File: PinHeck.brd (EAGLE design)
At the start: 359.2 x 152.3 mm, 337 parts, among them IC1 FT232RL-REEL, IC2 PIC32MX795F512L-80I/PT, IC3 CD74HCT244E, IC4 CD74HCT244E, IC5 ULN2803A, J1 500075-1517, J11 No Load, J2 500075-1517, J3 N/A, J6 161-3507-E, P1 TC33X-2-103E, SW1 101-0134-EV, SW2 101-0134-EV, U1 P8X32A-Q44, U10 74HCT2G04GV,125, U11 74HC165D,652, U12 74HC165D,652, U14 MC74HC08ADG, U15 MC74HC08ADG, U16 MC74HC08ADG, U17 MC74HC08ADG, U18 MC74HC08ADG, U19 MC74HC08ADG, U2 FT230XS-R, U20 TIP107, U21 TIP107, U22 TIP107, U23 TIP107, U24 TIP107, U25 TIP107, U26 TIP107, U27 TIP107, U28 TIP102, U29 TIP102, U3 74HC595D-Q100, U30 TIP102, U31 TIP102, U32 TIP102, U33 TIP102, U34 TIP102, U35 TIP102, U36 WS2801, U37 TIP102, U38 WS2801, U39 LM2937IMP-3.3/NOPB, U4 24LC1025-I/P, U40 TIP102, U41 TIP102, U42 TIP102, U43 TIP102, U44 TIP102, U45 TIP102, U46 TIP102, U47 TIP102, U48 TIP102, U49 TIP102, U5 74HC595D-Q100, U50 TIP102, U51 TIP102, U52 CD74HC123M96, U6 TIP102, U7 TIP102, U8 TIP102, U9 TIP102, X1 FQ7050B-8.000, X2 ECS-65-20-4X

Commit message: Updated Bill of Materials.
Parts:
- BOARD_POWER, SOL_PWR: value 26-62-4040 -> 26-60-4040
- C10: device PP_Passives:0805 -> PP_Passives:1206
- moved C10 0.80 mm to (95.8, 105.9)
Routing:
- net GND: track 54.5 -> 52.0 mm
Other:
- outline, holes or cut-outs redrawn
- board text added: "REV: 5"
- board text removed: "REV: 6"
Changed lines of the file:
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@@
 <?xml version="1.0" encoding="utf-8"?>
 <!DOCTYPE eagle SYSTEM "eagle.dtd">
-<eagle version="6.3">
+<eagle version="6.5.0">
 <drawing>
 <settings>
@@
 <wire x1="339.09" y1="174.371" x2="339.09" y2="22.098" width="0.4064" layer="20"/>
 <wire x1="339.09" y1="22.098" x2="-20.066" y2="22.098" width="0.4064" layer="20"/>
-<wire x1="-20.066" y1="22.098" x2="-20.066" y2="174.117" width="0.4064" layer="20"/>
-<wire x1="-20.066" y1="174.117" x2="-20.066" y2="174.371" width="0.4064" layer="20"/>
+<wire x1="-20.066" y1="22.098" x2="-20.066" y2="174.371" width="0.4064" layer="20"/>
 <text x="50.292" y="166.624" size="1.4224" layer="21" font="vector">PIC USB</text>
 <text x="80.518" y="158.242" size="1.016" layer="21" font="vector" rot="R90">AC_46</text>
@@
 <text x="316.992" y="110.998" size="0.8128" layer="21" font="vector">GND</text>
 <text x="235.204" y="108.712" size="1.016" layer="21">PinHeck Pinball System</text>
-<text x="235.204" y="107.188" size="1.016" layer="21">REV: 6</text>
+<text x="235.204" y="107.188" size="1.016" layer="21">REV: 5</text>
 <text x="235.204" y="102.362" size="1.016" layer="21">Designers:</text>
 <text x="235.204" y="105.664" size="1.016" layer="21">www.benheck.com</text>
@@
 <element name="C9" library="PP_Passives" package="0805" value=".1uF" x="104.648" y="133.096" rot="R180"/>
 <element name="C11" library="PP_Passives" package="0805" value=".1uF" x="86.614" y="133.858" rot="R180"/>
-<element name="C10" library="PP_Passives" package="0805" value="10uF" x="96.012" y="106.68" smashed="yes" rot="R270">
-<attribute name="NAME" x="95.123" y="104.2035" size="0.8128" layer="25" font="vector"/>
+<element name="C10" library="PP_Passives" package="1206" value="10uF" x="95.758" y="105.918" smashed="yes" rot="R270">
+<attribute name="NAME" x="93.345" y="108.5215" size="0.8128" layer="25" font="vector"/>
 </element>
 <element name="R12" library="PP_Passives" package="0805" value="50" x="125.222" y="115.57"/>
@@
 <element name="F2" library="PP_Passives" package="4245K" value="4245K" x="257.048" y="66.294" rot="R270"/>
 <element name="F3" library="PP_Passives" package="4245K" value="4245K" x="269.24" y="66.294" rot="R270"/>
-<element name="SOL_PWR" library="PP_Connectors" package="MOLEX_KK_4" value="26-62-4040" x="257.556" y="28.702" smashed="yes">
+<element name="SOL_PWR" library="PP_Connectors" package="MOLEX_KK_4" value="26-60-4040" x="257.556" y="28.702" smashed="yes">
 <attribute name="NAME" x="252.857" y="35.941" size="1.4224" layer="25" font="vector"/>
 </element>
@@
 <element name="C46" library="PP_Passives" package="0805" value=".1uF" x="227.33" y="133.858" rot="R270"/>
 <element name="C47" library="PP_Passives" package="0805" value=".1uF" x="193.04" y="133.858" rot="R270"/>
-<element name="BOARD_POWER" library="PP_Connectors" package="MOLEX_KK_4" value="26-62-4040" x="18.288" y="167.894" smashed="yes">
+<element name="BOARD_POWER" library="PP_Connectors" package="MOLEX_KK_4" value="26-60-4040" x="18.288" y="167.894" smashed="yes">
 <attribute name="NAME" x="10.033" y="160.909" size="1.4224" layer="25" font="vector"/>
 </element>
@@
 <wire x1="98.844" y1="127.35" x2="98.844" y2="132.372" width="0.1778" layer="1"/>
 <wire x1="98.844" y1="132.372" x2="99.314" y2="132.842" width="0.1778" layer="1"/>
-<wire x1="99.314" y1="132.842" x2="100.584" y2="132.842" width="0.1778" layer="1"/>
-<wire x1="100.584" y1="132.842" x2="101.092" y2="132.842" width="0.1778" layer="1"/>
-<wire x1="101.23" y1="133.488" x2="101.23" y2="133.858" width="0.1778" layer="1"/>
 <wire x1="103.748" y1="133.096" x2="103.494" y2="132.842" width="0.1778" layer="1"/>
-<wire x1="103.494" y1="132.842" x2="101.092" y2="132.842" width="0.1778" layer="1"/>
-<wire x1="101.23" y1="133.488" x2="101.23" y2="132.842" width="0.1778" layer="1"/>
-<wire x1="101.23" y1="132.842" x2="100.584" y2="132.842" width="0.1778" layer="1"/>
+<wire x1="103.494" y1="132.842" x2="99.314" y2="132.842" width="0.1778" layer="1"/>
+<wire x1="101.23" y1="133.858" x2="101.23" y2="132.842" width="0.1778" layer="1"/>
+<wire x1="101.23" y1="132.842" x2="101.092" y2="132.842" width="0.1778" layer="1"/>
 <wire x1="100.844" y1="127.35" x2="100.838" y2="127.344" width="0.1778" layer="1"/>
-<wire x1="100.838" y1="127.344" x2="100.838" y2="125.73" width="0.1778" layer="1"/>
-<wire x1="100.838" y1="125.73" x2="100.838" y2="129.286" width="0.1778" layer="1"/>
+<wire x1="100.838" y1="127.344" x2="100.838" y2="129.286" width="0.1778" layer="1"/>
 <wire x1="100.838" y1="129.286" x2="101.6" y2="130.048" width="0.1778" layer="1"/>
 <via x="102.616" y="133.35" extent="1-16" drill="0.5" diameter="0.8048"/>
 <via x="107.188" y="133.35" extent="1-16" drill="0.5" diameter="0.8048"/>
 <wire x1="104.744" y1="121.45" x2="103.67" y2="121.45" width="0.1778" layer="1"/>
-<wire x1="103.67" y1="121.45" x2="103.378" y2="121.158" width="0.1778" layer="1"/>
-<wire x1="100.838" y1="125.73" x2="100.838" y2="121.412" width="0.1778" layer="1"/>
+<wire x1="100.838" y1="127.344" x2="100.838" y2="121.412" width="0.1778" layer="1"/>
 <wire x1="100.838" y1="121.412" x2="101.6" y2="120.65" width="0.1778" layer="1"/>
 <wire x1="101.6" y1="120.65" x2="102.87" y2="120.65" width="0.1778" layer="1"/>
-<wire x1="102.87" y1="120.65" x2="103.378" y2="121.158" width="0.1778" layer="1"/>
+<wire x1="102.87" y1="120.65" x2="103.67" y2="121.45" width="0.1778" layer="1"/>
 <via x="122.428" y="125.73" extent="1-16" drill="0.5" diameter="0.8048"/>
 <via x="122.682" y="119.888" extent="1-16" drill="0.5" diameter="0.8048"/>
@@
 <contactref element="C50" pad="NEG"/>
 <via x="127" y="120.65" extent="1-16" drill="0.5" diameter="0.8048"/>
-<via x="94.742" y="105.664" extent="1-16" drill="0.5" diameter="0.8048"/>
-<via x="94.742" y="106.934" extent="1-16" drill="0.5" diameter="0.8048"/>
-<via x="94.742" y="108.204" extent="1-16" drill="0.5" diameter="0.8048"/>
+<via x="93.726" y="105.664" extent="1-16" drill="0.5" diameter="0.8048"/>
+<via x="93.726" y="104.14" extent="1-16" drill="0.5" diameter="0.8048"/>
+<via x="93.726" y="107.442" extent="1-16" drill="0.5" diameter="0.8048"/>
 <via x="104.14" y="105.41" extent="1-16" drill="0.5" diameter="0.8048"/>
 <via x="89.662" y="114.808" extent="1-16" drill="0.5" diameter="0.8048"/>
@@
 <via x="109.347" y="124.9045" extent="1-16" drill="0.5" diameter="0.8048"/>
 <via x="111.379" y="124.9045" extent="1-16" drill="0.5" diameter="0.8048"/>
-<wire x1="111.39" y1="121.45" x2="110.998" y2="121.45" width="0.1778" layer="1"/>
 <via x="112.395" y="121.8565" extent="1-16" drill="0.5" diameter="0.8048"/>
-<wire x1="110.998" y1="121.45" x2="104.744" y2="121.45" width="0.1778" layer="1"/>
+<wire x1="111.39" y1="121.45" x2="104.744" y2="121.45" width="0.1778" layer="1"/>
 <wire x1="111.39" y1="121.45" x2="112.268" y2="121.45" width="0.1778" layer="1"/>
 <wire x1="112.268" y1="121.45" x2="112.268" y2="121.92" width="0.1778" layer="1"/>
 <wire x1="111.39" y1="122.428" x2="111.39" y2="121.45" width="0.1778" layer="1"/>
-<wire x1="111.39" y1="121.45" x2="110.998" y2="121.45" width="0.1778" layer="1"/>
 <via x="104.902" y="113.792" extent="1-16" drill="0.5" diameter="0.8048"/>
 <via x="93.218" y="115.824" extent="1-16" drill="0.5" diameter="0.8048"/>
@@
 <contactref element="IC2" pad="85"/>
 <contactref element="C10" pad="1"/>
-<wire x1="96.012" y1="107.58" x2="96.012" y2="107.9801" width="0.2032" layer="1"/>
+<wire x1="95.758" y1="107.318" x2="96.012" y2="107.9801" width="0.2032" layer="1"/>
 <wire x1="96.844" y1="113.95" x2="96.844" y2="108.8121" width="0.2032" layer="1"/>
 <wire x1="96.844" y1="108.8121" x2="96.012" y2="107.9801" width="0.2032" layer="1"/>
@@
 <contactref element="R51" pad="2"/>
 <contactref element="IC2" pad="74"/>
-<wire x1="152.7835" y1="78.867" x2="153.0477" y2="78.867" width="0.254" layer="1"/>
 <wire x1="153.0477" y1="78.867" x2="153.924" y2="79.7433" width="0.254" layer="1"/>
 <wire x1="153.924" y1="79.7433" x2="153.924" y2="83.174" width="0.254" layer="1"/>
-<wire x1="151.504" y1="78.867" x2="152.7835" y2="78.867" width="0.254" layer="1"/>
-<wire x1="153.5843" y1="83.8535" x2="153.924" y2="83.5138" width="0.254" layer="1"/>
+<wire x1="151.504" y1="78.867" x2="153.0477" y2="78.867" width="0.254" layer="1"/>
 <wire x1="153.924" y1="83.5138" x2="153.924" y2="83.174" width="0.254" layer="1"/>
-<via x="89.408" y="104.648" extent="1-16" drill="0.5" diameter="0.8048"/>
+<via x="91.694" y="102.362" extent="1-16" drill="0.5" diameter="0.8048"/>
 <via x="87.884" y="114.3" extent="1-16" drill="0.5" diameter="0.8048"/>
-<wire x1="89.408" y1="104.648" x2="106.934" y2="104.648" width="0.254" layer="1"/>
-<wire x1="106.934" y1="104.648" x2="120.396" y2="91.186" width="0.254" layer="1"/>
+<wire x1="91.694" y1="102.362" x2="109.22" y2="102.362" width="0.254" layer="1"/>
+<wire x1="109.22" y1="102.362" x2="120.396" y2="91.186" width="0.254" layer="1"/>
 <wire x1="120.396" y1="91.186" x2="152.294790625" y2="91.186" width="0.254" layer="1"/>
 <wire x1="152.294790625" y1="91.186" x2="152.654" y2="90.826790625" width="0.254" layer="1"/>
 <wire x1="152.654" y1="90.826790625" x2="152.654" y2="84.7838" width="0.254" layer="1"/>
-<wire x1="152.654" y1="84.7838" x2="153.5843" y2="83.8535" width="0.254" layer="1"/>
+<wire x1="152.654" y1="84.7838" x2="153.924" y2="83.5138" width="0.254" layer="1"/>
 <wire x1="87.884" y1="114.3" x2="87.884" y2="106.172" width="0.254" layer="16"/>
-<wire x1="87.884" y1="106.172" x2="89.408" y2="104.648" width="0.254" layer="16"/>
+<wire x1="87.884" y1="106.172" x2="91.694" y2="102.362" width="0.254" layer="16"/>
 <wire x1="91.344" y1="116.25" x2="89.834" y2="116.25" width="0.1778" layer="1"/>
 <wire x1="89.834" y1="116.25" x2="87.884" y2="114.3" width="0.1778" layer="1"/>

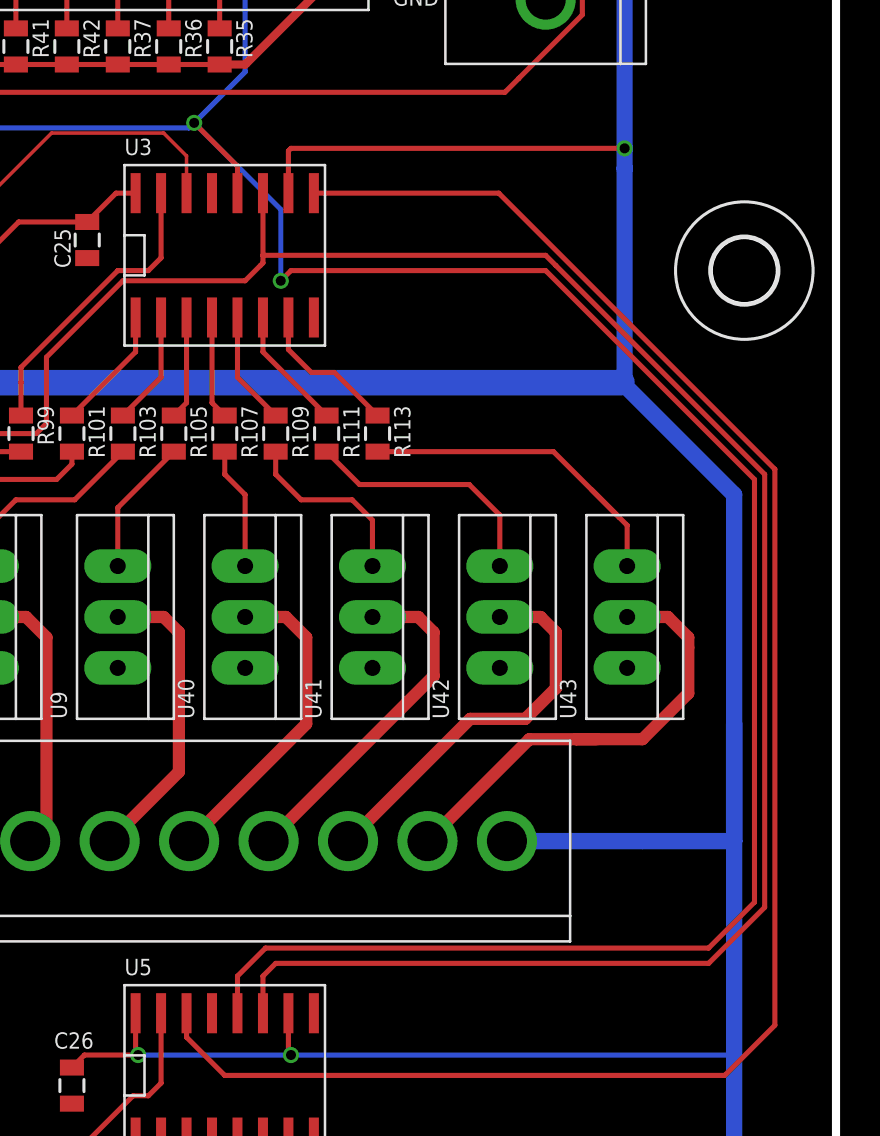
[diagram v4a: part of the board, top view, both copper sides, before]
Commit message: Swapped LAT and CLK on 595. FIXED.
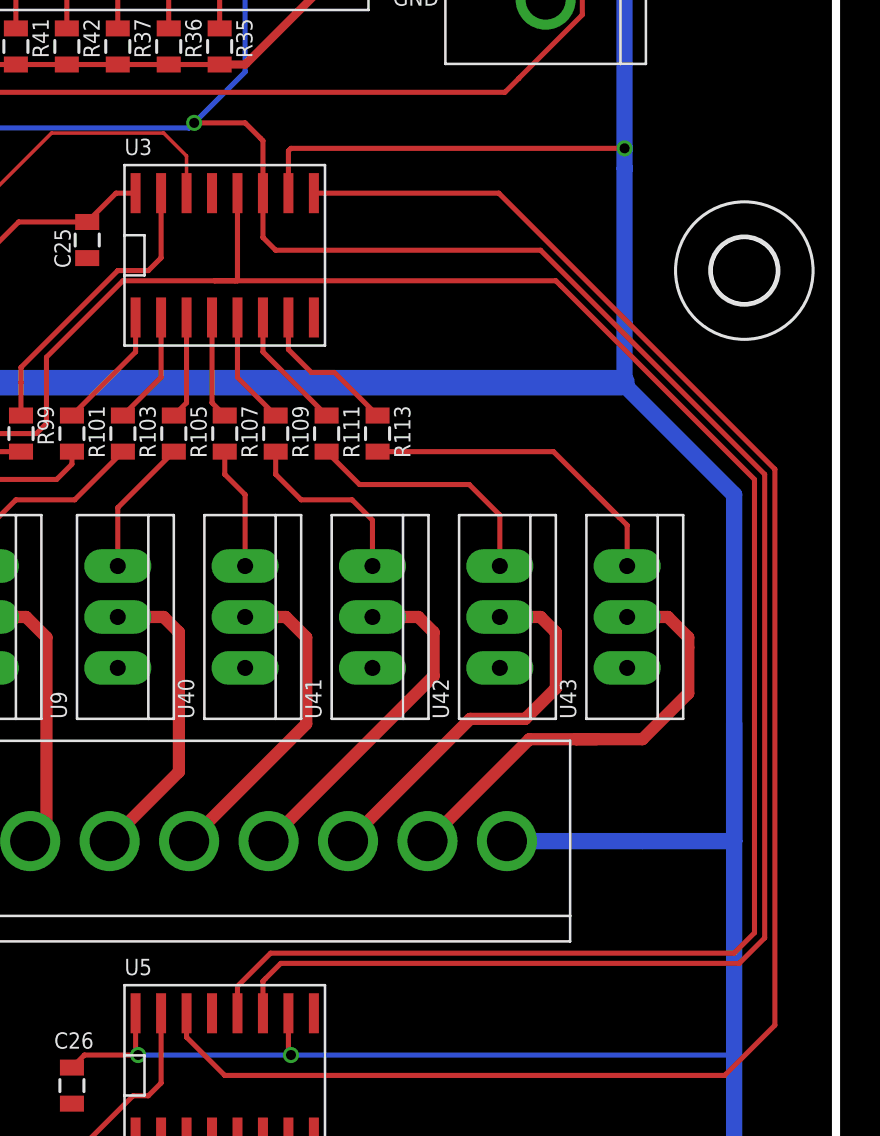
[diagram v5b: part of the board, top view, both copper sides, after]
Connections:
- net !DATA_LAT: now also U3.12, U5.12; no longer U3.11, U5.11
- net DATA_CLK: now also U3.11, U5.11; no longer U3.12, U5.12
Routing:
- net DATA_CLK: track 365.2 -> 361.9 mm, vias 4 -> 3
- net !DATA_LAT: track 115.6 -> 117.4 mm
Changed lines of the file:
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@@
 </signal>
 <signal name="DATA_CLK">
-<contactref element="U3" pad="12"/>
-<contactref element="U5" pad="12"/>
 <contactref element="U11" pad="2"/>
 <contactref element="U12" pad="2"/>
@@
 <wire x1="307.288" y1="129.413" x2="308.991" y2="129.413" width="0.254" layer="1"/>
 <wire x1="308.991" y1="129.413" x2="309.118" y2="129.286" width="0.254" layer="1" curve="-90"/>
-<wire x1="307.086" y1="105.156" x2="309.245" y2="102.997" width="0.254" layer="1"/>
-<wire x1="309.245" y1="102.997" x2="309.245" y2="101.652" width="0.254" layer="1"/>
 <wire x1="309.626" y1="115.062" x2="309.626" y2="110.744" width="0.254" layer="16"/>
 <wire x1="309.626" y1="110.744" x2="309.626" y2="107.696" width="0.254" layer="16"/>
 <wire x1="309.626" y1="107.696" x2="307.086" y2="105.156" width="0.254" layer="16"/>
 <via x="307.086" y="105.156" extent="1-16" drill="0.5"/>
-<wire x1="309.245" y1="60.758" x2="309.245" y2="62.611" width="0.254" layer="1"/>
-<wire x1="309.245" y1="62.611" x2="310.642" y2="64.008" width="0.254" layer="1"/>
-<wire x1="310.642" y1="64.008" x2="332.74" y2="64.008" width="0.254" layer="1"/>
-<wire x1="332.74" y1="64.008" x2="335.026" y2="66.294" width="0.254" layer="1"/>
-<wire x1="335.026" y1="66.294" x2="335.026" y2="87.376" width="0.254" layer="1"/>
-<wire x1="335.026" y1="87.376" x2="324.612" y2="97.79" width="0.254" layer="1"/>
-<wire x1="324.612" y1="97.79" x2="311.912" y2="97.79" width="0.254" layer="1"/>
-<wire x1="311.912" y1="97.79" x2="311.404" y2="97.282" width="0.254" layer="1"/>
-<via x="311.404" y="97.282" extent="1-16" drill="0.5"/>
-<wire x1="311.404" y1="97.282" x2="311.404" y2="100.838" width="0.254" layer="16"/>
-<wire x1="311.404" y1="100.838" x2="307.086" y2="105.156" width="0.254" layer="16"/>
 <wire x1="283.21" y1="104.902" x2="290.83" y2="104.902" width="0.254" layer="16"/>
 <wire x1="290.83" y1="104.902" x2="306.832" y2="104.902" width="0.254" layer="16"/>
 <wire x1="306.832" y1="104.902" x2="307.086" y2="105.156" width="0.254" layer="16"/>
+<contactref element="U5" pad="11"/>
+<contactref element="U3" pad="11"/>
+<wire x1="307.086" y1="105.156" x2="309.626" y2="105.156" width="0.254" layer="1"/>
+<wire x1="309.626" y1="105.156" x2="310.388" y2="104.394" width="0.254" layer="1"/>
+<wire x1="310.388" y1="104.394" x2="310.515" y2="104.267" width="0.254" layer="1"/>
+<wire x1="310.515" y1="104.267" x2="310.515" y2="101.652" width="0.254" layer="1"/>
+<wire x1="310.515" y1="101.652" x2="310.515" y2="99.441" width="0.254" layer="1"/>
+<wire x1="310.515" y1="99.441" x2="311.15" y2="98.806" width="0.254" layer="1"/>
+<wire x1="311.15" y1="98.806" x2="324.358" y2="98.806" width="0.254" layer="1"/>
+<wire x1="324.358" y1="98.806" x2="335.534" y2="87.63" width="0.254" layer="1"/>
+<wire x1="335.534" y1="87.63" x2="335.534" y2="64.516" width="0.254" layer="1"/>
+<wire x1="335.534" y1="64.516" x2="334.264" y2="63.246" width="0.254" layer="1"/>
+<wire x1="334.264" y1="63.246" x2="311.404" y2="63.246" width="0.254" layer="1"/>
+<wire x1="311.404" y1="63.246" x2="310.642" y2="62.484" width="0.254" layer="1"/>
+<wire x1="310.642" y1="62.484" x2="310.515" y2="62.357" width="0.254" layer="1"/>
+<wire x1="310.515" y1="62.357" x2="310.515" y2="60.758" width="0.254" layer="1"/>
 </signal>
 <signal name="GI_DATA_COL_B">
@@
 <signal name="!DATA_LAT">
 <contactref element="U10" pad="6"/>
-<contactref element="U3" pad="11"/>
-<contactref element="U5" pad="11"/>
 <wire x1="290.002" y1="100.1" x2="290.002" y2="96.078" width="0.254" layer="1"/>
 <wire x1="290.002" y1="96.078" x2="296.418" y2="89.662" width="0.254" layer="1"/>
@@
 <wire x1="299.72" y1="90.17" x2="299.72" y2="93.472" width="0.254" layer="1"/>
 <wire x1="299.72" y1="93.472" x2="303.53" y2="97.282" width="0.254" layer="1"/>
-<wire x1="303.53" y1="97.282" x2="309.626" y2="97.282" width="0.254" layer="1"/>
-<wire x1="309.626" y1="97.282" x2="310.388" y2="98.044" width="0.254" layer="1"/>
-<wire x1="310.388" y1="98.044" x2="310.515" y2="98.171" width="0.254" layer="1"/>
-<wire x1="310.515" y1="98.171" x2="310.515" y2="98.552" width="0.254" layer="1"/>
-<wire x1="310.515" y1="98.552" x2="310.515" y2="101.652" width="0.254" layer="1"/>
-<wire x1="310.515" y1="60.758" x2="310.515" y2="62.611" width="0.254" layer="1"/>
-<wire x1="310.515" y1="62.611" x2="311.15" y2="63.246" width="0.254" layer="1"/>
-<wire x1="311.15" y1="63.246" x2="332.74" y2="63.246" width="0.254" layer="1"/>
-<wire x1="332.74" y1="63.246" x2="335.534" y2="66.04" width="0.254" layer="1"/>
-<wire x1="335.534" y1="66.04" x2="335.534" y2="87.63" width="0.254" layer="1"/>
-<wire x1="335.534" y1="87.63" x2="325.12" y2="98.044" width="0.254" layer="1"/>
-<wire x1="325.12" y1="98.044" x2="324.612" y2="98.552" width="0.254" layer="1"/>
-<wire x1="324.612" y1="98.552" x2="310.515" y2="98.552" width="0.254" layer="1"/>
+<contactref element="U3" pad="12"/>
+<contactref element="U5" pad="12"/>
+<wire x1="303.53" y1="97.282" x2="308.102" y2="97.282" width="0.254" layer="1"/>
+<wire x1="308.102" y1="97.282" x2="309.118" y2="97.282" width="0.254" layer="1"/>
+<wire x1="309.245" y1="60.758" x2="309.245" y2="62.103" width="0.254" layer="1"/>
+<wire x1="309.245" y1="62.103" x2="310.896" y2="63.754" width="0.254" layer="1"/>
+<wire x1="310.896" y1="63.754" x2="334.01" y2="63.754" width="0.254" layer="1"/>
+<wire x1="334.01" y1="63.754" x2="335.026" y2="64.77" width="0.254" layer="1"/>
+<wire x1="335.026" y1="64.77" x2="335.026" y2="87.376" width="0.254" layer="1"/>
+<wire x1="335.026" y1="87.376" x2="325.374" y2="97.028" width="0.254" layer="1"/>
+<wire x1="325.374" y1="97.028" x2="325.12" y2="97.282" width="0.254" layer="1"/>
+<wire x1="325.12" y1="97.282" x2="309.118" y2="97.282" width="0.254" layer="1"/>
+<wire x1="309.245" y1="101.473" x2="309.245" y2="101.346" width="0.254" layer="1"/>
+<wire x1="309.245" y1="101.346" x2="309.245" y2="97.282" width="0.254" layer="1"/>
+<wire x1="309.245" y1="97.282" x2="308.102" y2="97.282" width="0.254" layer="1"/>
+<wire x1="309.245" y1="101.652" x2="309.245" y2="101.346" width="0.254" layer="1"/>
 </signal>
 <signal name="GI_DATA_COL">

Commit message: Changed names for unused IO
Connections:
- net ROW_ONE_DATA renamed RG9
- net ROW_ZERO_DATA renamed RG6
- new net RC1: IC2.6
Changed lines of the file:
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@@
 <?xml version="1.0" encoding="utf-8"?>
 <!DOCTYPE eagle SYSTEM "eagle.dtd">
-<eagle version="6.5.0">
+<eagle version="6.3">
 <drawing>
 <settings>
@@
 <wire x1="306.705" y1="59.563" x2="306.705" y2="60.758" width="0.254" layer="1"/>
 </signal>
-<signal name="ROW_ZERO_DATA">
+<signal name="RG6">
 <contactref element="IC2" pad="10"/>
 </signal>
-<signal name="ROW_ONE_DATA">
+<signal name="RG9">
 <contactref element="IC2" pad="14"/>
 </signal>
@@
 <wire x1="237.49" y1="70.104" x2="237.49" y2="72.644" width="0.4064" layer="1"/>
 </signal>
+<signal name="RC1">
+<contactref element="IC2" pad="6"/>
+</signal>
 </signals>
